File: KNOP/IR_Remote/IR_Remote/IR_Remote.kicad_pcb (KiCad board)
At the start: 2 copper layers, 2 parts, among them J1 Conn_01x01_Socket, J2 Conn_01x01_Socket

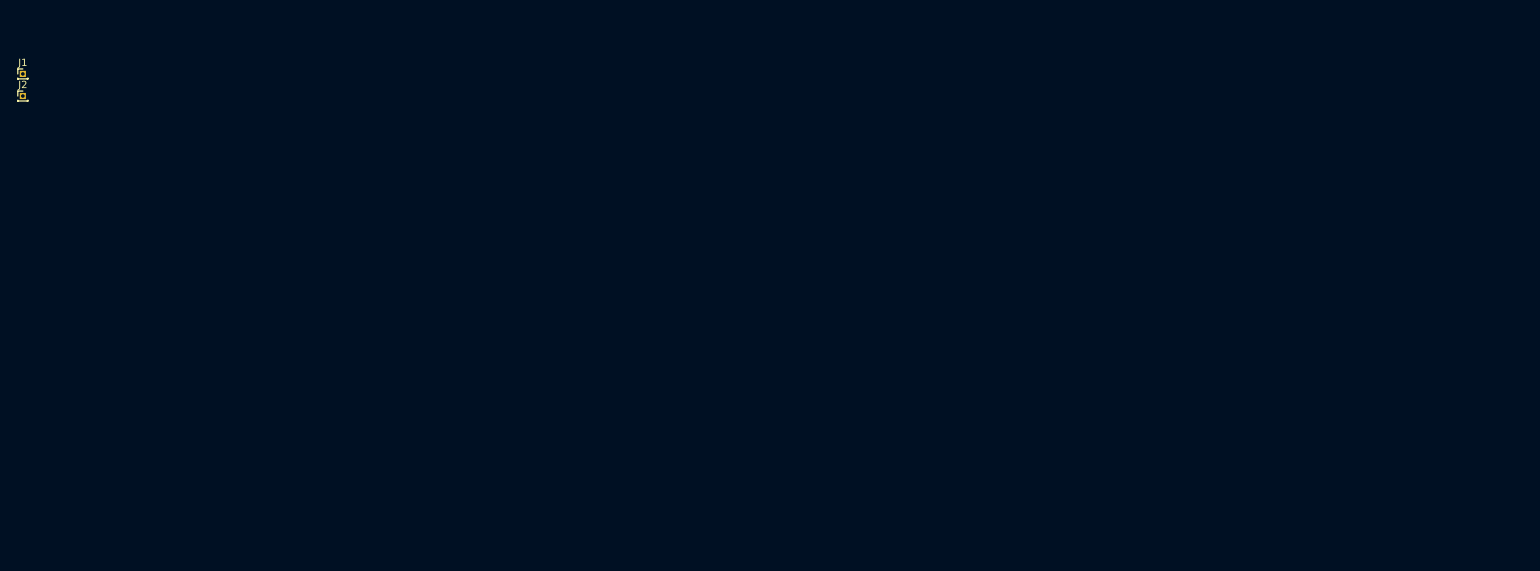
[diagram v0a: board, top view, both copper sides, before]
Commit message: IR Remote updates
IR RX and TX PCB updates
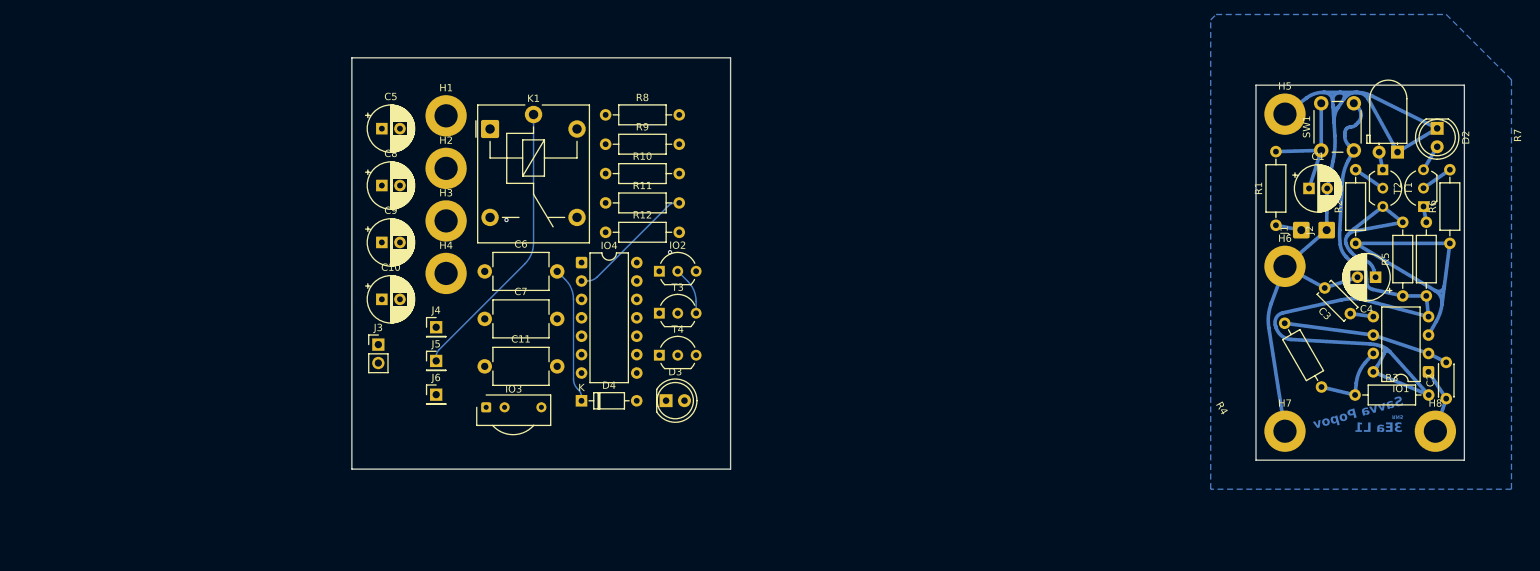
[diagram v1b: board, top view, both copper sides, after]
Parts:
- added C1: 100uF, Capacitor_THT:CP_Radial_D6.3mm_P2.50mm, F.Cu at (252.1, 68.8)
- added C10: 22uF, Capacitor_THT:CP_Radial_D6.3mm_P2.50mm, F.Cu at (124.1, 84.0)
- added C11: 100n, Capacitor_THT:C_Disc_D7.5mm_W5.0mm_P10.00mm, F.Cu at (138.3, 93.3)
- added C2: 100p, Capacitor_THT:C_Disc_D4.3mm_W1.9mm_P5.00mm, F.Cu at (271.0, 97.8)
- added C3: 2.2n, Capacitor_THT:C_Disc_D5.0mm_W2.5mm_P5.00mm, F.Cu at (257.8, 86.0)
- added C4: 10uF, Capacitor_THT:CP_Radial_D6.3mm_P2.50mm, F.Cu at (261.2, 81.0)
- added C5: 100uF, Capacitor_THT:CP_Radial_D6.3mm_P2.50mm, F.Cu at (124.1, 60.5)
- added C6: 100n, Capacitor_THT:C_Disc_D7.5mm_W5.0mm_P10.00mm, F.Cu at (138.3, 80.2)
- added C7: 100n, Capacitor_THT:C_Disc_D7.5mm_W5.0mm_P10.00mm, F.Cu at (138.3, 86.8)
- added C8: 100uF, Capacitor_THT:CP_Radial_D6.3mm_P2.50mm, F.Cu at (124.1, 68.3)
- added C9: 47uF, Capacitor_THT:CP_Radial_D6.3mm_P2.50mm, F.Cu at (124.1, 76.2)
- added D1: IR_LED, LED_THT:LED_D5.0mm_Horizontal_O1.27mm_Z3.0mm_Clear, F.Cu at (264.3, 63.7)
- added D2: Y_LED, LED_THT:LED_D5.0mm, F.Cu at (269.8, 60.5)
- added D3: R_LED, LED_THT:LED_D5.0mm, F.Cu at (163.4, 98.0)
- added D4: 1N4148, Diode_THT:D_DO-35_SOD27_P7.62mm_Horizontal, F.Cu at (151.7, 98.0)
- added H1: M3, MountingHole:MountingHole_3.2mm_M3_ISO7380_Pad, F.Cu at (133.0, 58.7)
- added H2: M3, MountingHole:MountingHole_3.2mm_M3_ISO7380_Pad, F.Cu at (133.0, 66.0)
- added H3: M3, MountingHole:MountingHole_3.2mm_M3_ISO7380_Pad, F.Cu at (133.0, 73.2)
- added H4: M3, MountingHole:MountingHole_3.2mm_M3_ISO7380_Pad, F.Cu at (133.0, 80.5)
- added H5: M3, MountingHole:MountingHole_3.2mm_M3_ISO7380_Pad, F.Cu at (248.8, 58.5)
- added H6: M3, MountingHole:MountingHole_3.2mm_M3_ISO7380_Pad, F.Cu at (248.8, 79.5)
- added H7: M3, MountingHole:MountingHole_3.2mm_M3_ISO7380_Pad, F.Cu at (248.8, 102.2)
- added H8: M3, MountingHole:MountingHole_3.2mm_M3_ISO7380_Pad, F.Cu at (269.5, 102.2)
- added IO1: NE555P, Package_DIP:DIP-8_W7.62mm, F.Cu at (268.6, 94.1)
- added IO2: L78L05_TO92, Package_TO_SOT_THT:TO-92_Inline_Wide, F.Cu at (162.4, 80.2)
- added IO3: TSOP312xx, OptoDevice:Vishay_CAST-3Pin, F.Cu at (138.5, 99.0)
- added IO4: 7490, Package_DIP:DIP-14_W7.62mm, F.Cu at (151.7, 79.0)
- added J3: Conn_01x02_Pin, Connector_PinHeader_2.54mm:PinHeader_1x02_P2.54mm_Vertical, F.Cu at (123.7, 90.3)
- added J4: Conn_01x01_Pin, Connector_PinHeader_2.54mm:PinHeader_1x01_P2.54mm_Vertical, F.Cu at (131.6, 87.9)
- added J5: Conn_01x01_Pin, Connector_PinHeader_2.54mm:PinHeader_1x01_P2.54mm_Vertical, F.Cu at (131.6, 92.5)
- added J6: Conn_01x01_Pin, Connector_PinHeader_2.54mm:PinHeader_1x01_P2.54mm_Vertical, F.Cu at (131.6, 97.2)
- added K1: Relay_SPDT, Relay_THT:Relay_SPDT_Finder_36.11, F.Cu at (139.1, 60.5)
- added R1: 47R, Resistor_THT:R_Axial_DIN0207_L6.3mm_D2.5mm_P10.16mm_Horizontal, F.Cu at (247.5, 73.8)
- added R10: 10k, Resistor_THT:R_Axial_DIN0207_L6.3mm_D2.5mm_P10.16mm_Horizontal, F.Cu at (155.0, 66.7)
- added R11: 470R, Resistor_THT:R_Axial_DIN0207_L6.3mm_D2.5mm_P10.16mm_Horizontal, F.Cu at (155.0, 70.8)
- added R12: 10k, Resistor_THT:R_Axial_DIN0207_L6.3mm_D2.5mm_P10.16mm_Horizontal, F.Cu at (155.0, 74.8)
- added R2: 47R, Resistor_THT:R_Axial_DIN0207_L6.3mm_D2.5mm_P10.16mm_Horizontal, F.Cu at (258.5, 76.3)
- added R3: 220k, Resistor_THT:R_Axial_DIN0207_L6.3mm_D2.5mm_P10.16mm_Horizontal, F.Cu at (258.4, 97.2)
- added R4: 22k, Resistor_THT:R_Axial_DIN0207_L6.3mm_D2.5mm_P10.16mm_Horizontal, F.Cu at (253.8, 96.1)
- added R5: 10R, Resistor_THT:R_Axial_DIN0207_L6.3mm_D2.5mm_P10.16mm_Horizontal, F.Cu at (265.0, 83.6)
- added R6: 2.2k, Resistor_THT:R_Axial_DIN0207_L6.3mm_D2.5mm_P10.16mm_Horizontal, F.Cu at (271.5, 76.3)
- added R7: 470R, Resistor_THT:R_Axial_DIN0207_L6.3mm_D2.5mm_P10.16mm_Horizontal, F.Cu at (268.2, 73.4)
- added R8: 10k, Resistor_THT:R_Axial_DIN0207_L6.3mm_D2.5mm_P10.16mm_Horizontal, F.Cu at (155.0, 58.6)
- added R9: 470R, Resistor_THT:R_Axial_DIN0207_L6.3mm_D2.5mm_P10.16mm_Horizontal, F.Cu at (155.0, 62.6)
- added SW1: SW_Push, Button_Switch_THT:SW_PUSH_6mm_H5mm, F.Cu at (253.8, 63.5)
- added T1: BC327, Package_TO_SOT_THT:TO-92_Inline_Wide, F.Cu at (262.2, 66.2)
- added T2: BC337, Package_TO_SOT_THT:TO-92_Inline_Wide, F.Cu at (267.9, 71.2)
- added T3: BC547, Package_TO_SOT_THT:TO-92_Inline_Wide, F.Cu at (162.4, 86.0)
- added T4: BC547, Package_TO_SOT_THT:TO-92_Inline_Wide, F.Cu at (162.4, 91.8)
- J1, J2: value Conn_01x01_Socket -> Conn_01x01_Pin; footprint Connector_PinHeader_1.00mm:PinHeader_1x01_P1.00mm_Vertical -> Connector_Wire:SolderWire-0.5sqmm_1x01_D0.9mm_OD2.3mm
- moved J2 180.8 mm to (254.5, 74.5), turned to 90 degrees
- moved J1 177.7 mm to (251.0, 74.5), turned to 90 degrees
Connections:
- J1 pad 1: GNDD -> Net-(J1-Pin_1)
- J2 pad 1: GND_TEST -> GND
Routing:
- net GND: track 0.00 -> 120.8 mm
- net VCC: track 0.00 -> 101.0 mm
- net OUTPUT_A: track 0.00 -> 42.7 mm
- net Net-(J5-Pin_1): track 0.00 -> 39.3 mm
- net Net-(T1-E): track 0.00 -> 25.8 mm
- net TR: track 0.00 -> 23.1 mm
- net +12V: track 0.00 -> 18.9 mm
- net Net-(C1-Pad1): track 0.00 -> 18.3 mm
- net Net-(IO4-R0(1)): track 0.00 -> 17.8 mm
- net Net-(IO1-DIS): track 0.00 -> 11.2 mm
- net GND1: track 0.00 -> 6.65 mm
- net OUTPUT_B: track 0.00 -> 4.53 mm
- net Net-(T2-B): track 0.00 -> 4.44 mm
- net Net-(D2-A): track 0.00 -> 3.69 mm
- net Net-(J1-Pin_1): track 0.00 -> 3.56 mm
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- added copper zone on B.Cu, net GND
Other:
- board outline added: 153.5 x 56.8 mm
- board text added: "3Ea L1"
- board text added: "RNS"
- board text added: "Savva Popov"

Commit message: PCB updates
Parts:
- C11, C6, C7: footprint Capacitor_THT:C_Disc_D7.5mm_W5.0mm_P10.00mm -> Capacitor_THT:C_Disc_D4.3mm_W1.9mm_P5.00mm
- moved H1 57.1 mm to (167.8, 104.0)
- moved R8 43.5 mm to (155.5, 102.1), turned to 90 degrees
- moved C9 40.1 mm to (160.5, 93.0), turned to -90 degrees
- moved H2 34.7 mm to (167.2, 71.8)
- moved D4 30.3 mm to (125.2, 83.4), turned to 30 degrees
- moved C8 29.1 mm to (153.1, 71.8)
- moved K1 28.6 mm to (128.8, 87.3)
- moved H4 25.4 mm to (123.5, 104.0)
- moved IO2 24.8 mm to (138.6, 73.2), turned to -165 degrees
- moved C11 22.4 mm to (149.8, 74.0), turned to 180 degrees
- moved D3 22.3 mm to (159.7, 76.0)
- moved C6 21.6 mm to (125.8, 97.8), turned to 90 degrees
- moved R9 20.9 mm to (165.1, 81.0), turned to 180 degrees
- moved J4 18.4 mm to (138.5, 105.0)
- moved C7 16.5 mm to (144.8, 71.6)
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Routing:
- net GND1: track 6.65 -> 264.3 mm
- net +5V: track 0.00 -> 77.8 mm
- net Net-(D4-A): track 0.00 -> 41.2 mm
- net +12V: track 18.9 -> 45.4 mm
- net NPN_C: track 0.00 -> 26.0 mm
- net Net-(J5-Pin_1): track 39.3 -> 19.7 mm
- net Net-(T4-B): track 0.00 -> 16.9 mm
- net Net-(T3-B): track 0.00 -> 14.2 mm, vias 1 -> 0
- net Net-(J4-Pin_1): track 0.00 -> 5.97 mm, vias 1 -> 0
- net Net-(J6-Pin_1): track 0.00 -> 5.92 mm
- net Net-(D3-A): track 0.00 -> 5.75 mm
- net TSOP_OUT: track 0.00 -> 4.27 mm
- net Net-(IO4-R0(1)): track 17.8 -> 20.5 mm
- net Q0: track 0.00 -> 2.51 mm
- added copper zone on B.Cu, net GND1
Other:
- board size 153.5 x 56.8 mm -> 153.5 x 53 mm

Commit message: charlies sd
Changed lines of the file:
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@@
 		(fp_line
 			(start 6.580001 0)
-			(end 5.929999 0)
+			(end 5.929999 0.000001)
 			(stroke
 				(width 0.12)
@@
 		)
 		(fp_text user "K"
-			(at 0 -1.799999 30)
+			(at 0.000001 -1.799999 30)
 			(layer "F.SilkS")
 			(effects
@@
 		)
 		(fp_text user "K"
-			(at 0 -1.799999 30)
+			(at 0.000001 -1.799999 30)
 			(layer "F.Fab")
 			(effects
@@
 		)
 		(fp_arc
-			(start 4.864182 1.122794)
+			(start 4.864181 1.122794)
 			(mid 4.633902 1.509327)
 			(end 4.340001 1.849999)
@@
 		)
 		(fp_arc
-			(start 2.54 -2.599999)
+			(start 2.54 -2.6)
 			(mid 3.93698 -2.192817)
 			(end 4.896402 -1.098806)
@@
 			(start 0.1836 -1.098807)
 			(mid 1.14302 -2.192817)
-			(end 2.54 -2.599999)
+			(end 2.54 -2.6)
 			(stroke
 				(width 0.12)
@@
 		)
 		(fp_line
-			(start 1.81 -3.181999)
+			(start 1.81 -3.181998)
 			(end 1.81 -1.04)
 			(stroke
@@
 		)
 		(fp_line
-			(start 3.050999 -2.69)
+			(start 3.050998 -2.69)
 			(end 3.051 -1.04)
 			(stroke
@@
 		(fp_line
 			(start 3.331 1.04)
-			(end 3.330999 2.484)
+			(end 3.330998 2.484)
 			(stroke
 				(width 0.12)
@@
 	(segment
 		(start 144.434894 100.724375)
-		(end 154.429377 103.12305)
+		(end 155.212156 103.310917)
 		(width 0.5)
 		(layer "B.Cu")
@@
 	)
 	(segment
-		(start 156.981167 102.216934)
+		(start 156.492163 102.856399)
 		(end 158.21 100.61)
 		(width 0.5)
@@
 	)
 	(arc
-		(start 156.981167 102.216934)
-		(mid 155.839668 103.048476)
-		(end 154.429377 103.12305)
+		(start 156.492163 102.856399)
+		(mid 155.919574 103.27351)
+		(end 155.212156 103.310917)
 		(width 0.5)
 		(layer "B.Cu")
